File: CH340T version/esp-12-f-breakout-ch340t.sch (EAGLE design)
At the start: 21 parts, among them IC1 REG1117, Q1 12.000

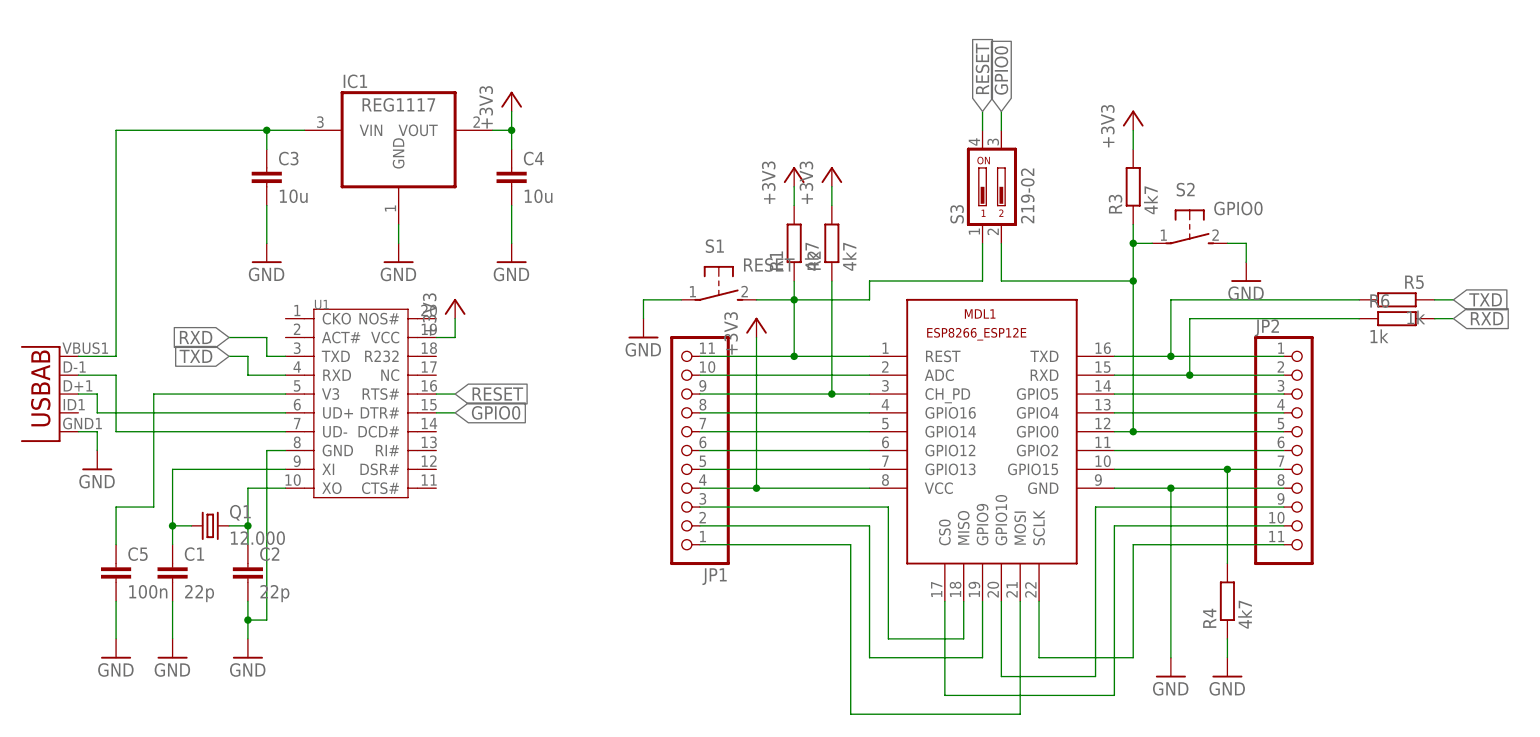
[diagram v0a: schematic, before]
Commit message: USB +5V pin added to pin headers
- Additional GND pin added
- Stabilizer layout rearranged
- Vias diameter slightly increased
- Drill-aid (0.4 mm) added
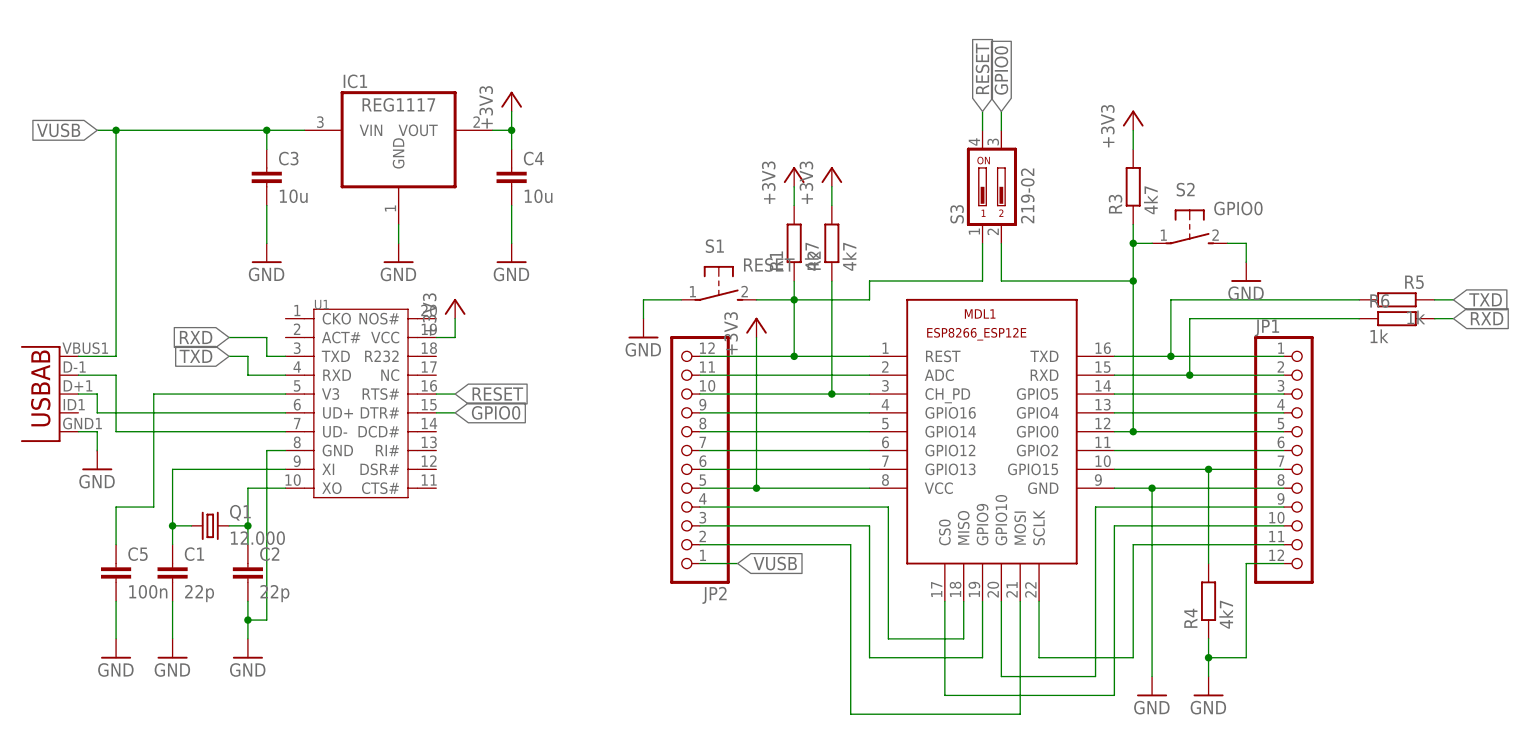
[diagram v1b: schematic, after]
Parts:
- JP1, JP2: device pinhead:PINHD-1X11 -> pinhead:PINHD-1X12
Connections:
- removed net N$27: C3.1, IC1.VIN, U2.VBUS
- new net VUSB: C3.1, IC1.VIN, JP2.1, U2.VBUS
- net +3V3: now also JP2.5; no longer JP1.4
- net GND: now also JP1.12, JP1.8; no longer JP2.8
- net N$1: now also JP2.12; no longer JP1.11
- net N$11: now also JP2.3; no longer JP1.2
- net N$12: now also JP1.9; no longer JP2.9
- net N$13: now also JP1.10; no longer JP2.10
- net N$14: now also JP1.11; no longer JP2.11
- net N$15: now also JP2.2; no longer JP1.1
- net N$16: now also JP1.7; no longer JP2.7
- net N$17: now also JP1.6; no longer JP2.6
- net N$18: now also JP1.5; no longer JP2.5
- net N$19: now also JP1.4; no longer JP2.4
- net N$2: now also JP2.11; no longer JP1.10
- net N$20: now also JP1.3; no longer JP2.3
- net N$21: now also JP1.2; no longer JP2.2
- net N$22: now also JP1.1; no longer JP2.1
- net N$3: now also JP2.10; no longer JP1.9
- net N$4: now also JP2.9; no longer JP1.8
- net N$5: now also JP2.8; no longer JP1.7
- net N$6: now also JP2.7; no longer JP1.6
- net N$7: now also JP2.6; no longer JP1.5
- net N$8: now also JP2.4; no longer JP1.3
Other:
- moved on the sheet: R4
